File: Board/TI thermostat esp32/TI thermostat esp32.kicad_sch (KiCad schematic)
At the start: 81 parts, among them IC1 ESP32-WROVER-E_M213EH6464PH3Q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, IC2 LT1074CT, J1 bme280, J4 Conn_02x05_Odd_Even, J5 Conn_02x03_Odd_Even, J6 Conn_01x08, Q1 BT134-600, Q2 BT134-600, Q3 BT134-600, Q4 BT134-600, SW1 SW_Push, U1 MOC3063M, U2 MOC3063M, U3 MOC3063M, U4 MOC3063M, U5 74HC00, U6 MAX7219, U7 74HC00, U8 LD1117S33TR_SOT223, U9 74HC138

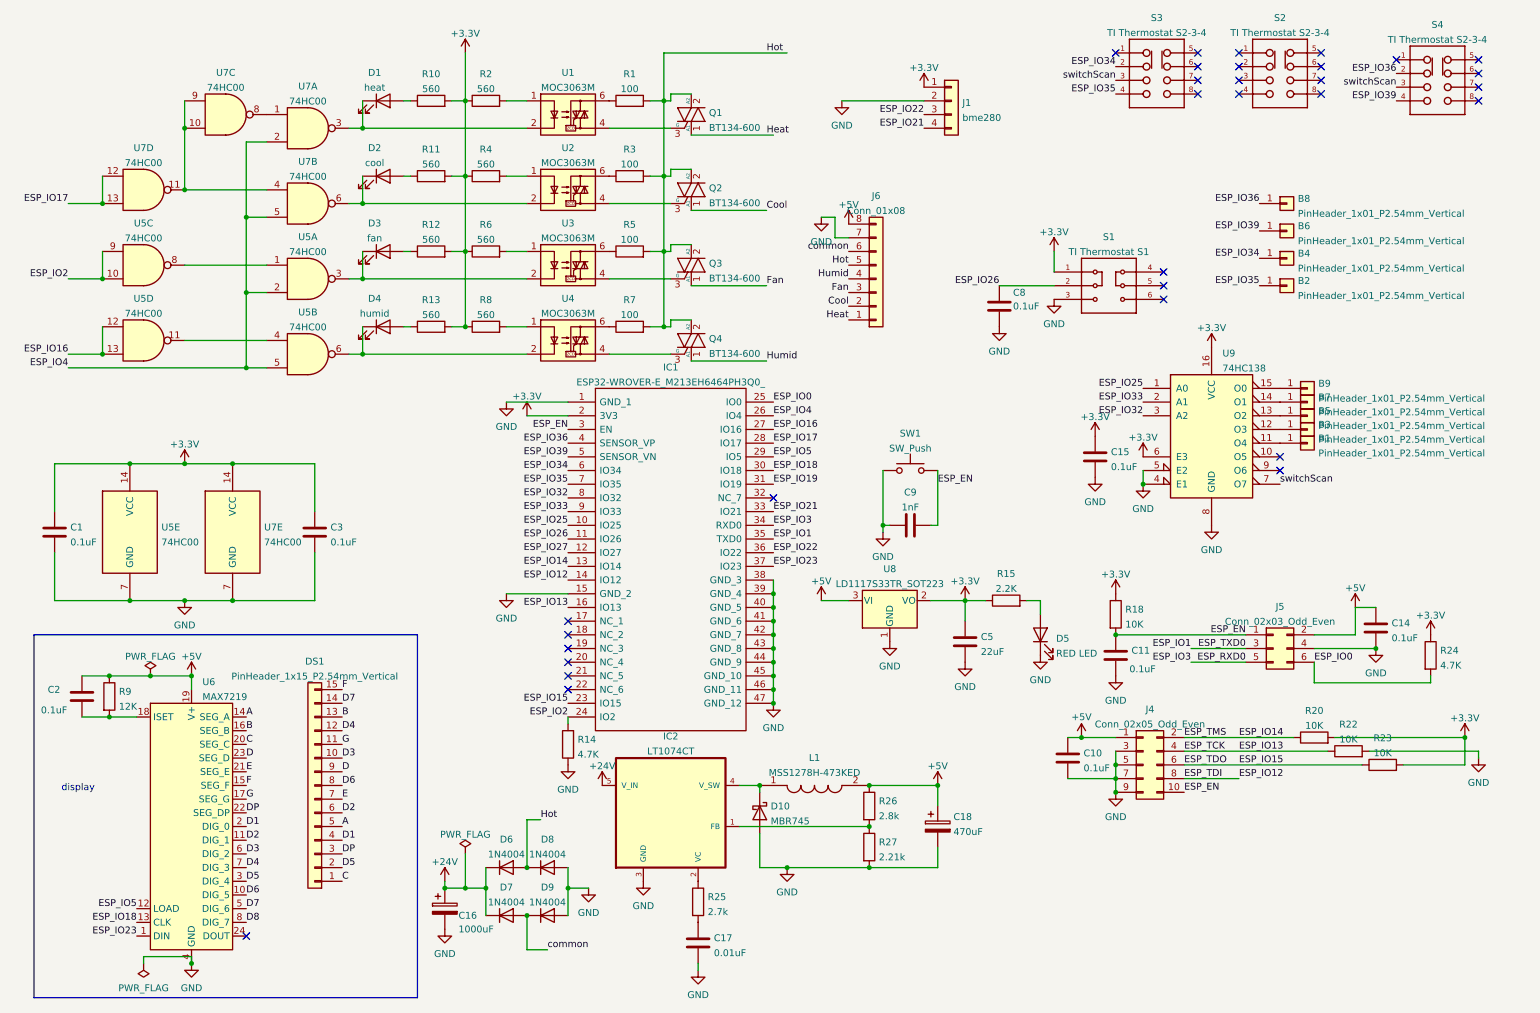
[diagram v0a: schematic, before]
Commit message: rev2 pcb and layout plus test code
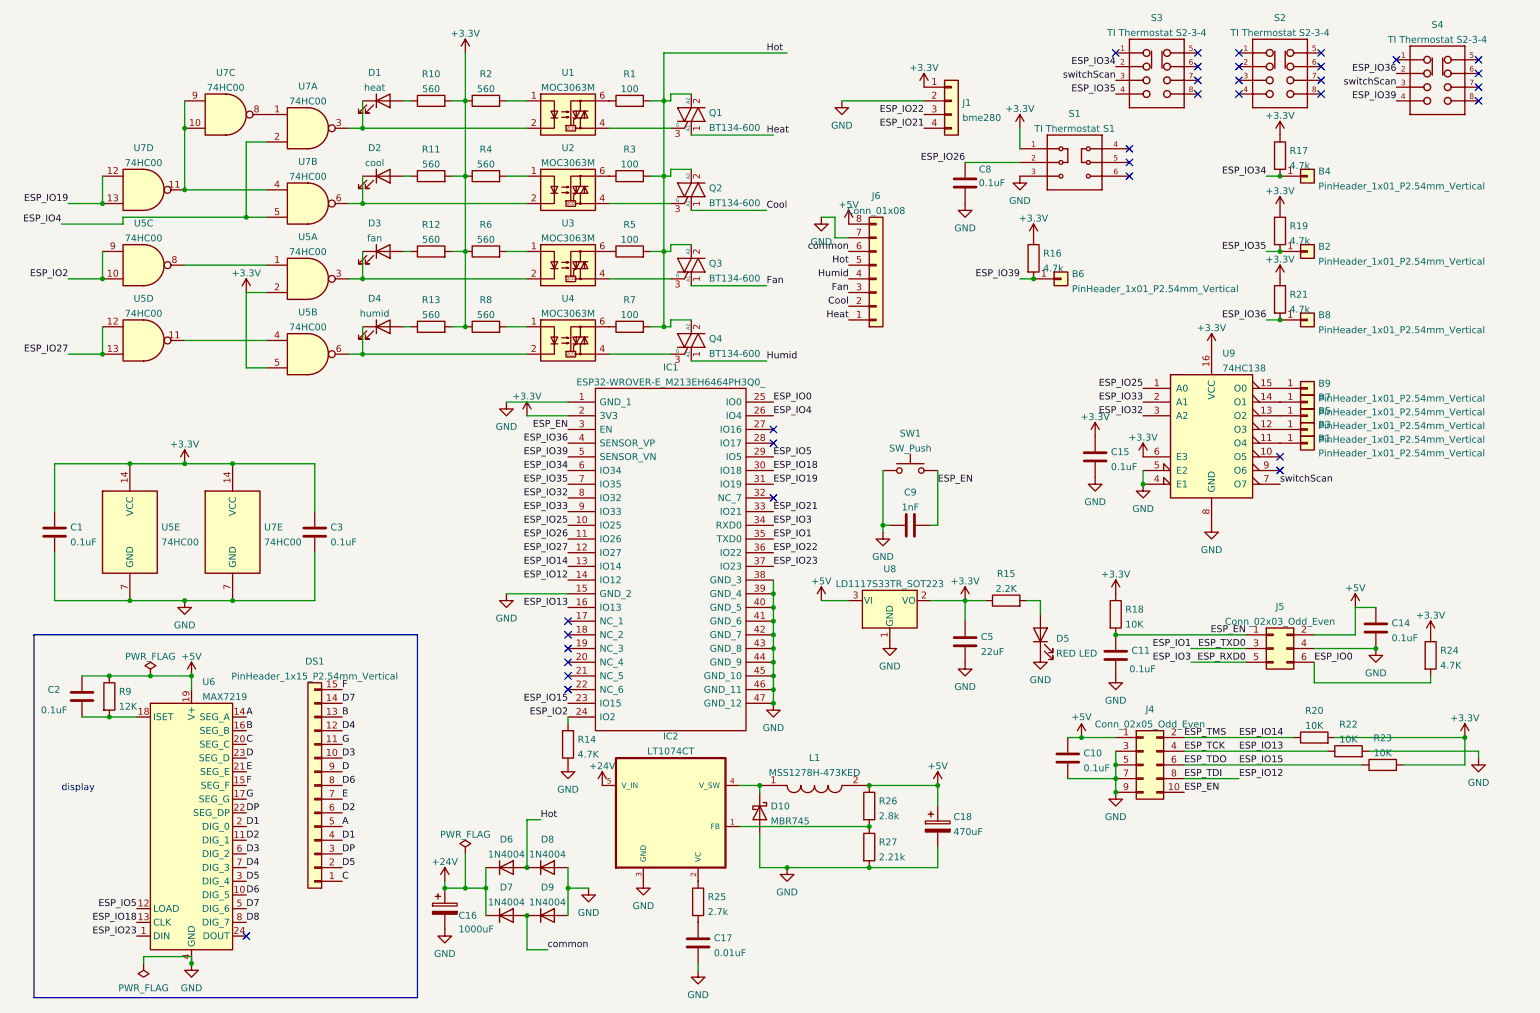
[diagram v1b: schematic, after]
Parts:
- added R16, R17, R19, R21: 4.7k, Resistor_SMD:R_0603_1608Metric, symbol Device:R
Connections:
- net +3V3: now also U5.2, U5.5, R16.1, R17.1, R19.1, R21.1
- net ESP_IO19: now also U7.12, U7.13
- net ESP_IO27: now also U5.12, U5.13
- net ESP_IO34: now also R17.2
- net ESP_IO35: now also R19.2
- net ESP_IO36: now also R21.2
- net ESP_IO39: now also R16.2
- net ESP_IO4: no longer U5.2, U5.5
- removed net ESP_IO16: IC1.27 (IO16), U5.12, U5.13
- removed net ESP_IO17: IC1.28 (IO17), U7.12, U7.13
- no-connect marks 31 -> 33
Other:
- moved on the sheet: B2, B4, B6, B8, C8, S1
